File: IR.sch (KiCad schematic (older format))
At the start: 6 parts, among them U47 74LS245, U48 74LS173, U49 74LS173, U50 74LS245, U51 74LS173, U52 74LS173

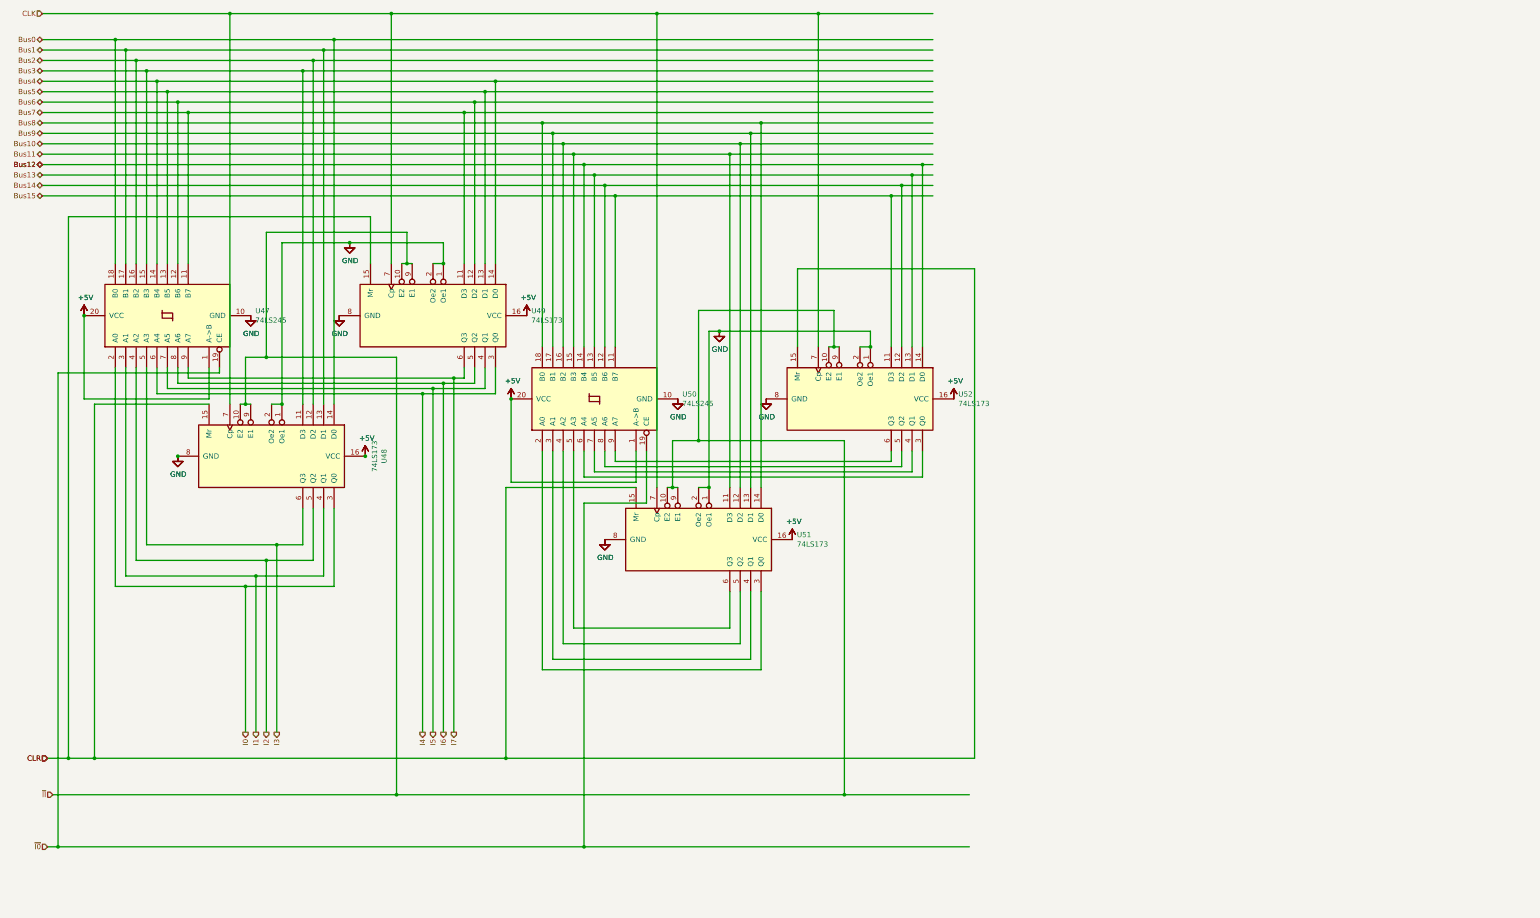
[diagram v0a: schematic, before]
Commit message: Added 8 bit output to the ir
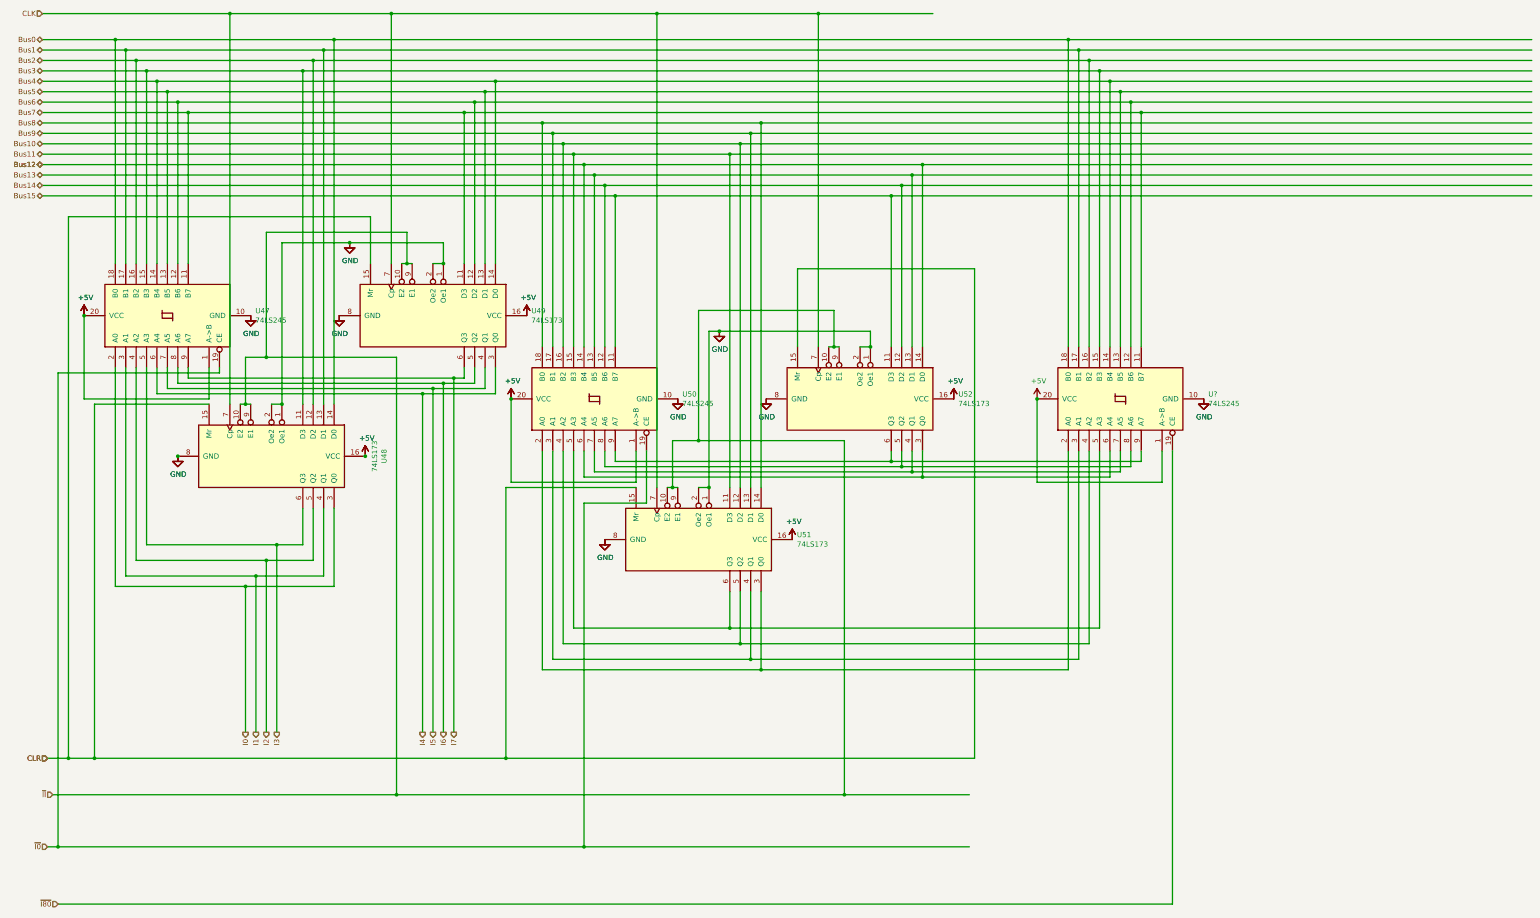
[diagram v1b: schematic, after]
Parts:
- added U?: 74LS245, Package_DIP:DIP-20_W7.62mm, symbol 16bitCpu-rescue:74LS245-74xx
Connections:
- net labels added: ~I80
- wire segments 219 -> 256
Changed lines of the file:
@@
 Connection ~ 4750 1250
-Wire Wire Line
-	4550 1450 10500 1450
-Wire Wire Line
-	4450 1550 10500 1550
-Wire Wire Line
-	4650 1350 10500 1350
-Wire Wire Line
-	4750 1250 10500 1250
 Wire Wire Line
 	2650 6500 3900 6500
@@
 Connection ~ 6300 1650
 Wire Wire Line
-	6300 1650 10500 1650
-Wire Wire Line
-	6200 1750 10500 1750
-Wire Wire Line
-	6100 1850 10500 1850
-Wire Wire Line
-	6000 1950 10500 1950
-Wire Wire Line
 	1950 2150 6850 2150
 Wire Wire Line
@@
 Connection ~ 7450 2750
 Connection ~ 8550 2350
-Wire Wire Line
-	8550 2350 10500 2350
 Connection ~ 8650 2250
-Wire Wire Line
-	8650 2250 10500 2250
 Connection ~ 8750 2150
-Wire Wire Line
-	8750 2150 10500 2150
 Connection ~ 8850 2050
-Wire Wire Line
-	8850 2050 10500 2050
 Wire Wire Line
 	8750 6550 8750 7200
@@
 CLR
 Wire Wire Line
-	6750 7300 8850 7300
-Wire Wire Line
 	6850 7200 8750 7200
 Wire Wire Line
@@
 Connection ~ 10400 2450
 Wire Wire Line
-	10400 2450 10500 2450
-Wire Wire Line
 	10300 2550 10300 4200
 Connection ~ 10300 2550
 Wire Wire Line
-	10300 2550 10500 2550
-Wire Wire Line
 	10200 4200 10200 2650
 Connection ~ 10200 2650
 Wire Wire Line
-	10200 2650 10500 2650
-Wire Wire Line
 	10100 4200 10100 2750
 Connection ~ 10100 2750
 Wire Wire Line
-	10100 2750 10500 2750
-Wire Wire Line
 	7250 5400 10300 5400
 Wire Wire Line
@@
 Wire Wire Line
 	10100 5300 7450 5300
+Wire Wire Line
+	4750 1250 11800 1250
+Wire Wire Line
+	4650 1350 11900 1350
+Wire Wire Line
+	4550 1450 12000 1450
+Wire Wire Line
+	4450 1550 12100 1550
+Wire Wire Line
+	6300 1650 12200 1650
+Wire Wire Line
+	6200 1750 12300 1750
+Wire Wire Line
+	8850 2050 16250 2050
+Wire Wire Line
+	8750 2150 16250 2150
+Wire Wire Line
+	8650 2250 16250 2250
+Wire Wire Line
+	8550 2350 16250 2350
+Wire Wire Line
+	10400 2450 16250 2450
+Wire Wire Line
+	10300 2550 16250 2550
+Wire Wire Line
+	10200 2650 16250 2650
+Wire Wire Line
+	10100 2750 16250 2750
+$Comp
+L 16bitCpu-rescue:GND-power #PWR?
+U 1 1 600A759A
+P 13100 4700
+AR Path="/600A759A" Ref="#PWR?"  Part="1"
+AR Path="/5F67C726/600A759A" Ref="#PWR?"  Part="1"
+AR Path="/5F70885A/600A759A" Ref="#PWR?"  Part="1"
+AR Path="/5F733C5E/600A759A" Ref="#PWR?"  Part="1"
+AR Path="/602D4838/600A759A" Ref="#PWR?"  Part="1"
+AR Path="/603B00C8/600A759A" Ref="#PWR?"  Part="1"
+AR Path="/603B766D/600A759A" Ref="#PWR?"  Part="1"
+AR Path="/5F74778C/600A759A" Ref="#PWR?"  Part="1"
+AR Path="/5F79B702/600A759A" Ref="#PWR?"  Part="1"
+F 0 "#PWR?" H 13100 4450 50  0001 C CNN
+F 1 "GND" H 13105 4527 50  0000 C CNN
+F 2 "" H 13100 4700 50  0001 C CNN
+F 3 "" H 13100 4700 50  0001 C CNN
+	1    13100 4700
+	1    0    0    -1
+$EndComp
+$Comp
+L 16bitCpu-rescue:GND-power #PWR?
+U 1 1 600A75A1
+P 13100 4700
+AR Path="/600A75A1" Ref="#PWR?"  Part="1"
+AR Path="/5F67C726/600A75A1" Ref="#PWR?"  Part="1"
+AR Path="/5F70885A/600A75A1" Ref="#PWR?"  Part="1"
+AR Path="/5F733C5E/600A75A1" Ref="#PWR?"  Part="1"
+AR Path="/602D4838/600A75A1" Ref="#PWR?"  Part="1"
+AR Path="/603B00C8/600A75A1" Ref="#PWR?"  Part="1"
+AR Path="/603B766D/600A75A1" Ref="#PWR?"  Part="1"
+AR Path="/5F74778C/600A75A1" Ref="#PWR?"  Part="1"
+AR Path="/5F79B702/600A75A1" Ref="#PWR?"  Part="1"
+F 0 "#PWR?" H 13100 4450 50  0001 C CNN
+F 1 "GND" H 13105 4527 50  0000 C CNN
+F 2 "" H 13100 4700 50  0001 C CNN
+F 3 "" H 13100 4700 50  0001 C CNN
+	1    13100 4700
+	1    0    0    -1
+$EndComp
+$Comp
+L 16bitCpu-rescue:74LS245-74xx U?
+U 1 1 600A75A7
+P 12300 4700
+AR Path="/600A75A7" Ref="U?"  Part="1"
+AR Path="/5F67C726/600A75A7" Ref="U?"  Part="1"
+AR Path="/5F70885A/600A75A7" Ref="U?"  Part="1"
+AR Path="/5F733C5E/600A75A7" Ref="U?"  Part="1"
+AR Path="/602D4838/600A75A7" Ref="U?"  Part="1"
+AR Path="/603B00C8/600A75A7" Ref="U?"  Part="1"
+AR Path="/603B766D/600A75A7" Ref="U?"  Part="1"
+AR Path="/5F74778C/600A75A7" Ref="U?"  Part="1"
+AR Path="/5F79B702/600A75A7" Ref="U?"  Part="1"
+F 0 "U?" V 12346 3856 50  0000 R CNN
+F 1 "74LS245" V 12255 3856 50  0000 R CNN
+F 2 "Package_DIP:DIP-20_W7.62mm" H 12300 4700 50  0001 C CNN
+F 3 "http://www.ti.com/lit/gpn/sn74LS245" H 12300 4700 50  0001 C CNN
+	1    12300 4700
+	0    -1   -1   0
+$EndComp
+$Comp
+L 16bitCpu-rescue:+5V-power #PWR?
+U 1 1 600BC57F
+P 11500 4700
+AR Path="/600BC57F" Ref="#PWR?"  Part="1"
+AR Path="/5F67C726/600BC57F" Ref="#PWR?"  Part="1"
+AR Path="/5F70885A/600BC57F" Ref="#PWR?"  Part="1"
+AR Path="/5F733C5E/600BC57F" Ref="#PWR?"  Part="1"
+AR Path="/602D4838/600BC57F" Ref="#PWR?"  Part="1"
+AR Path="/603B00C8/600BC57F" Ref="#PWR?"  Part="1"
+AR Path="/603B766D/600BC57F" Ref="#PWR?"  Part="1"
+AR Path="/5F74778C/600BC57F" Ref="#PWR?"  Part="1"
+AR Path="/5F79B702/600BC57F" Ref="#PWR?"  Part="1"
+F 0 "#PWR?" H 11500 4550 50  0001 C CNN
+F 1 "+5V" H 11515 4873 50  0000 C CNN
+F 2 "" H 11500 4700 50  0001 C CNN
+F 3 "" H 11500 4700 50  0001 C CNN
+	1    11500 4700
+	1    0    0    -1
+$EndComp
+Wire Wire Line
+	11800 4200 11800 1250
+Connection ~ 11800 1250
+Wire Wire Line
+	11800 1250 16250 1250
+Wire Wire Line
+	11900 4200 11900 1350
+Connection ~ 11900 1350
+Wire Wire Line
+	11900 1350 16250 1350
+Wire Wire Line
+	12000 4200 12000 1450
+Connection ~ 12000 1450
+Wire Wire Line
+	12000 1450 16250 1450
+Connection ~ 12100 1550
+Wire Wire Line
+	12100 1550 16250 1550
+Wire Wire Line
+	12100 1550 12100 4200
+Wire Wire Line
+	12200 4200 12200 1650
+Connection ~ 12200 1650
+Wire Wire Line
+	12200 1650 16250 1650
+Wire Wire Line
+	12300 4200 12300 1750
+Connection ~ 12300 1750
+Wire Wire Line
+	12300 1750 16250 1750
+Wire Wire Line
+	6000 1950 12500 1950
+Wire Wire Line
+	6100 1850 12400 1850
+Wire Wire Line
+	12400 4200 12400 1850
+Connection ~ 12400 1850
+Wire Wire Line
+	12400 1850 16250 1850
+Wire Wire Line
+	12500 4200 12500 1950
+Connection ~ 12500 1950
+Wire Wire Line
+	12500 1950 16250 1950
+Wire Wire Line
+	10100 5300 12500 5300
+Wire Wire Line
+	12500 5300 12500 5200
+Connection ~ 10100 5300
+Wire Wire Line
+	10200 5350 12400 5350
+Wire Wire Line
+	12400 5350 12400 5200
+Connection ~ 10200 5350
+Wire Wire Line
+	10300 5400 12300 5400
+Wire Wire Line
+	12300 5400 12300 5200
+Connection ~ 10300 5400
+Wire Wire Line
+	10400 5450 12200 5450
+Wire Wire Line
+	12200 5450 12200 5200
+Connection ~ 10400 5450
+Wire Wire Line
+	11800 7300 11800 5200
+Wire Wire Line
+	6750 7300 8850 7300
+Connection ~ 8850 7300
+Wire Wire Line
+	8850 7300 11800 7300
+Wire Wire Line
+	8750 7200 11900 7200
+Wire Wire Line
+	11900 7200 11900 5200
+Connection ~ 8750 7200
+Wire Wire Line
+	8650 7050 12000 7050
+Wire Wire Line
+	12000 7050 12000 5200
+Connection ~ 8650 7050
+Wire Wire Line
+	8550 6900 12100 6900
+Wire Wire Line
+	12100 6900 12100 5200
+Connection ~ 8550 6900
+Wire Wire Line
+	12700 5200 12700 5500
+Wire Wire Line
+	12700 5500 11500 5500
+Wire Wire Line
+	11500 5500 11500 4700
+Connection ~ 11500 4700
+Wire Wire Line
+	2100 9550 12800 9550
+Wire Wire Line
+	12800 9550 12800 5200
+Text HLabel 2100 9550 0    50   Input ~ 0
+~I80
 $EndSCHEMATC

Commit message: Let there be light
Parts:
- gave numbers to parts that had none: 1
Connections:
- wire segments 256 -> 292
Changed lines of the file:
@@
 $Descr A3 16535 11693
 encoding utf-8
-Sheet 8 11
+Sheet 13 20
 Title ""
 Date ""
@@
 	2850 6250 4100 6250
 Wire Wire Line
-	3350 4500 5900 4500
+	3350 4500 5300 4500
 Connection ~ 6000 1950
 Connection ~ 6100 1850
@@
 	5900 4500 6000 4500
 Wire Wire Line
-	3250 4550 5800 4550
+	3250 4550 5400 4550
 Connection ~ 5800 4550
 Wire Wire Line
@@
 	5800 7900 5800 4550
 Wire Wire Line
-	3150 4600 5700 4600
+	3150 4600 5450 4600
 Connection ~ 5700 4600
 Wire Wire Line
@@
 	5600 7900 5600 4650
 Wire Wire Line
-	3050 4650 5600 4650
+	3050 4650 5500 4650
 Connection ~ 5600 4650
 Wire Wire Line
@@
 AR Path="/603B766D/600A759A" Ref="#PWR?"  Part="1"
 AR Path="/5F74778C/600A759A" Ref="#PWR?"  Part="1"
-AR Path="/5F79B702/600A759A" Ref="#PWR?"  Part="1"
-F 0 "#PWR?" H 13100 4450 50  0001 C CNN
+AR Path="/5F79B702/600A759A" Ref="#PWR0182"  Part="1"
+F 0 "#PWR0182" H 13100 4450 50  0001 C CNN
 F 1 "GND" H 13105 4527 50  0000 C CNN
 F 2 "" H 13100 4700 50  0001 C CNN
@@
 AR Path="/603B766D/600A75A1" Ref="#PWR?"  Part="1"
 AR Path="/5F74778C/600A75A1" Ref="#PWR?"  Part="1"
-AR Path="/5F79B702/600A75A1" Ref="#PWR?"  Part="1"
-F 0 "#PWR?" H 13100 4450 50  0001 C CNN
+AR Path="/5F79B702/600A75A1" Ref="#PWR0240"  Part="1"
+F 0 "#PWR0240" H 13100 4450 50  0001 C CNN
 F 1 "GND" H 13105 4527 50  0000 C CNN
 F 2 "" H 13100 4700 50  0001 C CNN
@@
 AR Path="/603B766D/600A75A7" Ref="U?"  Part="1"
 AR Path="/5F74778C/600A75A7" Ref="U?"  Part="1"
-AR Path="/5F79B702/600A75A7" Ref="U?"  Part="1"
-F 0 "U?" V 12346 3856 50  0000 R CNN
+AR Path="/5F79B702/600A75A7" Ref="U75"  Part="1"
+F 0 "U75" V 12346 3856 50  0000 R CNN
 F 1 "74LS245" V 12255 3856 50  0000 R CNN
 F 2 "Package_DIP:DIP-20_W7.62mm" H 12300 4700 50  0001 C CNN
@@
 AR Path="/603B766D/600BC57F" Ref="#PWR?"  Part="1"
 AR Path="/5F74778C/600BC57F" Ref="#PWR?"  Part="1"
-AR Path="/5F79B702/600BC57F" Ref="#PWR?"  Part="1"
-F 0 "#PWR?" H 11500 4550 50  0001 C CNN
+AR Path="/5F79B702/600BC57F" Ref="#PWR0181"  Part="1"
+F 0 "#PWR0181" H 11500 4550 50  0001 C CNN
 F 1 "+5V" H 11515 4873 50  0000 C CNN
 F 2 "" H 11500 4700 50  0001 C CNN
@@
 Text HLabel 2100 9550 0    50   Input ~ 0
 ~I80
+$Sheet
+S 1050 6250 550  1800
+U 621E2556
+F0 "sheet621E2544" 50
+F1 "led16.sch" 50
+F2 "I0" I R 1600 6500 50
+F3 "I1" I R 1600 6600 50
+F4 "I2" I R 1600 6700 50
+F5 "I3" I R 1600 6800 50
+F6 "I4" I R 1600 6900 50
+F7 "I5" I R 1600 7000 50
+F8 "I6" I R 1600 7100 50
+F9 "I7" I R 1600 7200 50
+F10 "I8" I R 1600 7300 50
+F11 "I9" I R 1600 7400 50
+F12 "I10" I R 1600 7500 50
+F13 "I11" I R 1600 7600 50
+F14 "I12" I R 1600 7700 50
+F15 "I13" I R 1600 7800 50
+F16 "I14" I R 1600 7900 50
+F17 "I15" I R 1600 8000 50
+$EndSheet
+Wire Wire Line
+	1600 6500 2650 6500
+Connection ~ 2650 6500
+Wire Wire Line
+	1600 6600 2750 6600
+Wire Wire Line
+	2750 6600 2750 6400
+Connection ~ 2750 6400
+Wire Wire Line
+	1600 6700 2850 6700
+Wire Wire Line
+	2850 6700 2850 6250
+Connection ~ 2850 6250
+Wire Wire Line
+	2950 6100 2950 6800
+Wire Wire Line
+	2950 6800 1600 6800
+Connection ~ 2950 6100
+Wire Wire Line
+	1600 6900 5500 6900
+Connection ~ 5500 4650
+Wire Wire Line
+	5500 4650 5600 4650
+Wire Wire Line
+	5500 6900 5500 4650
+Wire Wire Line
+	1600 7000 5450 7000
+Wire Wire Line
+	5450 7000 5450 4600
+Connection ~ 5450 4600
+Wire Wire Line
+	5450 4600 5700 4600
+Wire Wire Line
+	1600 7100 5400 7100
+Wire Wire Line
+	5400 7100 5400 4550
+Connection ~ 5400 4550
+Wire Wire Line
+	5400 4550 5800 4550
+Wire Wire Line
+	1600 7200 5300 7200
+Wire Wire Line
+	5300 7200 5300 4500
+Connection ~ 5300 4500
+Wire Wire Line
+	5300 4500 5900 4500
+Wire Wire Line
+	1600 7300 6750 7300
+Connection ~ 6750 7300
+Wire Wire Line
+	1600 7400 6850 7400
+Wire Wire Line
+	6850 7400 6850 7200
+Connection ~ 6850 7200
+Wire Wire Line
+	1600 7500 6950 7500
+Wire Wire Line
+	6950 7500 6950 7050
+Connection ~ 6950 7050
+Wire Wire Line
+	7050 6900 7050 7600
+Wire Wire Line
+	7050 7600 1600 7600
+Connection ~ 7050 6900
+Wire Wire Line
+	1600 7700 10400 7700
+Wire Wire Line
+	10400 7700 10400 5450
+Wire Wire Line
+	10300 5400 10300 7800
+Wire Wire Line
+	10300 7800 1600 7800
+Wire Wire Line
+	1750 7900 1750 7850
+Wire Wire Line
+	1750 7850 8650 7850
+Wire Wire Line
+	8650 7850 8650 7050
+Wire Wire Line
+	1600 7900 1750 7900
+Wire Wire Line
+	8550 6900 8550 8000
+Wire Wire Line
+	8550 8000 1600 8000
 $EndSCHEMATC
